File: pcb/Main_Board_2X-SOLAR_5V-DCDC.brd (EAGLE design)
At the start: 82.6 x 29.8 mm, 32 parts, among them T2 MMUN2133LT1G, U1 LTC4015EUHFPBFQFN-38_UHF-M, U3 TPS61090RSAR, X1 6V_PV, X2 5V output

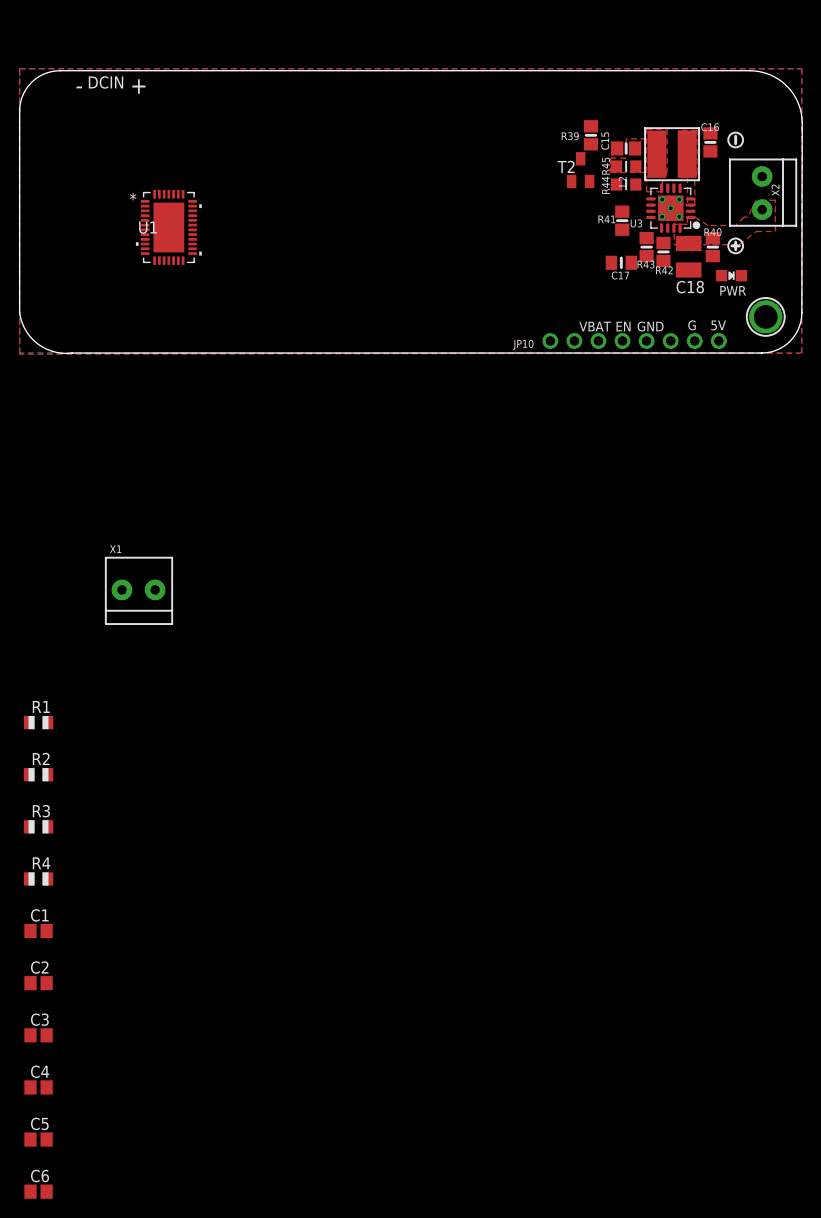
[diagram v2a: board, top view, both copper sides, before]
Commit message: Updated BOM and layout for LTC4015
Schematic pinout redone for LTC4015 part to match design application guide and make schematic easier to follow. Schematic and board routing started. BOM updated and consolidated for last revision of board (non-LTC)
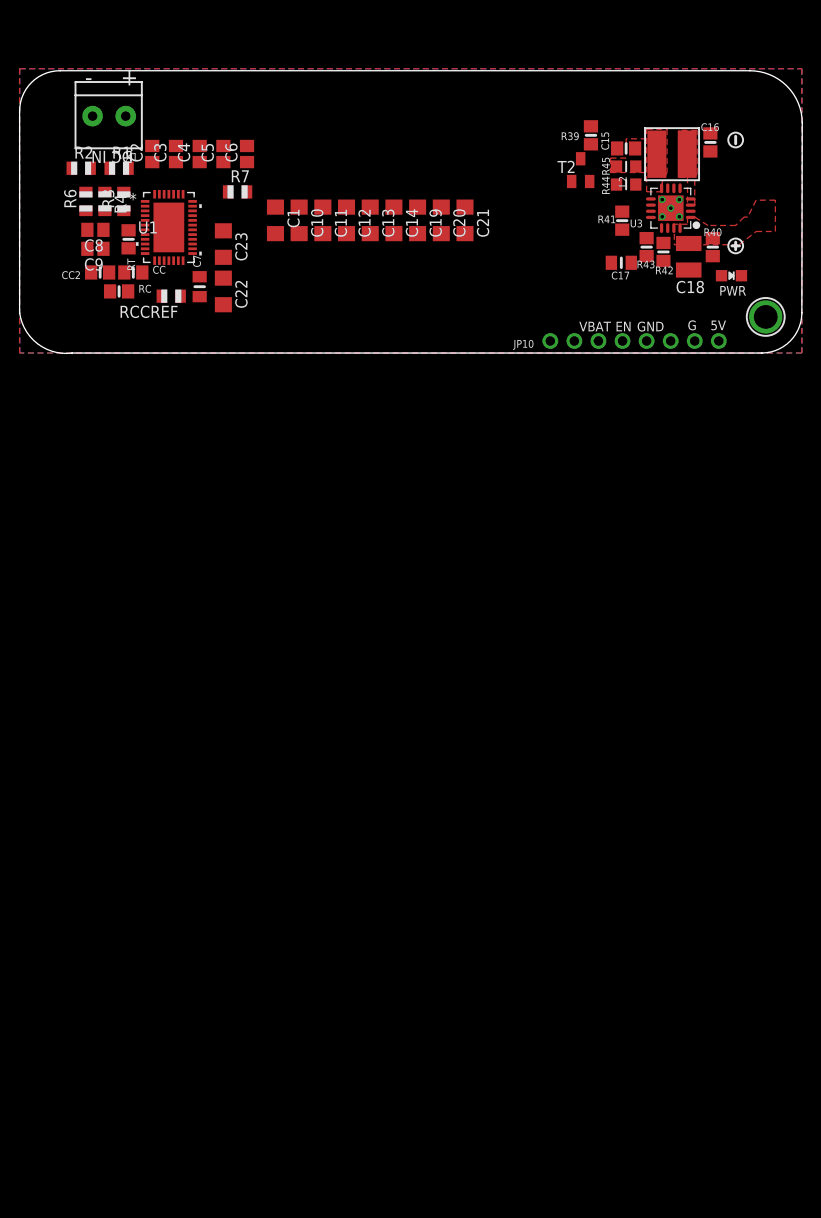
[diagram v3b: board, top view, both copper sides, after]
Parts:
- removed X2: 5V output, microbuilder:TERMBLOCK_1X2-3.5MM
- added C10, C11, C12, C13, C14, C19, C20, C22: 10 uF, resistor:C1206
- added C21, C23: 0.1 uF, resistor:C1206
- added C7: 0.1uF, microbuilder:0805_10MGAP
- added C8: 0.1 uF, adafruit:C0805
- added C9: 10 uF, adafruit:C0805
- added CC: 0.22 uF, microbuilder:0805-NO
- added CC2: 0.01 uF, microbuilder:0805-NO
- added R6, R7: 10k, adafruit:R0805
- added RC: 200, microbuilder:0805-NO
- added RCCREF: 301k, adafruit:R0805
- added RT: 95.3k, microbuilder:0805-NO
- C1: value (none) -> 10 uF; device adafruit:C0805 -> resistor:C1206
- C2, C3, C4, C5: value (none) -> 10 uF
- C6: value (none) -> 100 pF
- R1: value (none) -> 47k
- R2: value (none) -> 10k
- R3: value (none) -> 226k
- R4: value (none) -> 64.9k
- moved C6 111.7 mm to (24.0, 21.0), turned to 90 degrees
- moved C5 105.8 mm to (21.5, 21.0), turned to 90 degrees
- moved C4 100.0 mm to (19.0, 21.0), turned to 90 degrees
- moved C3 94.1 mm to (16.5, 21.0), turned to 90 degrees
- moved C2 88.3 mm to (14.0, 21.0), turned to 90 degrees
- moved C1 79.1 mm to (27.0, 14.0), turned to 270 degrees
- moved R4 71.8 mm to (9.00, 16.0), turned to 270 degrees
- moved R3 66.6 mm to (11.0, 16.0), turned to 90 degrees
- moved R2 64.2 mm to (6.50, 19.5)
- moved R1 59.1 mm to (10.5, 19.5)
- moved X1 50.1 mm to (9.50, 25.0), turned to 180 degrees
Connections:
- net N$42 renamed FB
- net N$44 renamed LED+
- removed net GND_2: U1.14
- removed net SGND: U1.7
- new net INTVCC: C8.1, C9.1, U1.27, U1.28, U1.36, U1.38
- new net N$1: C6.1, R7.2, U1.8
- new net N$11: CC.2, RC.2
- new net N$12: C23.1, U1.25
- new net N$2: C2.1, C3.1, C4.1, C5.1, R1.2, R3.2, U1.35, X1.1
- new net N$3: R3.1, R4.2
- new net N$4: R4.1, R6.2, R7.1
- new net N$5: R1.1, R2.2
- new net N$6: C7.1, RCCREF.1, U1.17
- new net N$8: RT.2, U1.10
- new net N$9: CC.1, CC2.1, U1.9
- new net SCL: U1.4
- new net SDA: U1.5
- new net SMBALERT: U1.6
- new net SYS: C1.1, C10.1, C11.1, C12.1, C13.1, C14.1, C15.1, C17.1, C19.1, C20.1, C21.1, L2.P$1, R45.2, U1.31, U3.8
- net 5.0V: no longer X2.2
- net GND: now also C1.2, C10.2, C11.2, C12.2, C13.2, C14.2, C19.2, C2.2, C20.2, C21.2, C23.2, C3.2, C4.2, C5.2, C6.2, C7.2, C8.2, C9.2, CC2.2, R2.1, R6.1, RC.1, RCCREF.2, RT.1, U1.14, U1.23, U1.37, U1.7, X1.2; no longer X1.1, X2.1
- net VBAT: no longer C15.1, C17.1, L2.P$1, R45.2, U3.8
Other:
- board text added: "DC IN"
- board text removed: "DCIN"

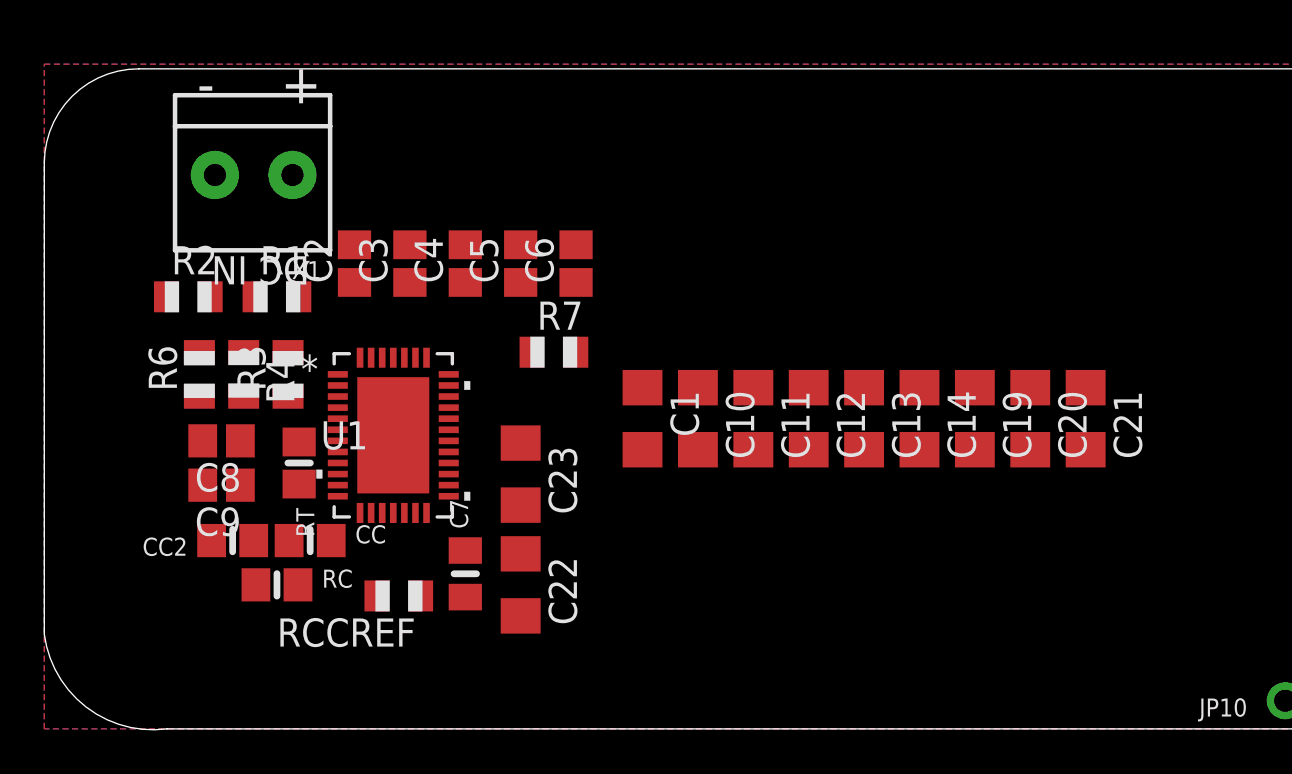
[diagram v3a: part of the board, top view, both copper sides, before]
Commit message: Updated library, schematic, and board layout
Added new components to library and continuing to update schematic and board
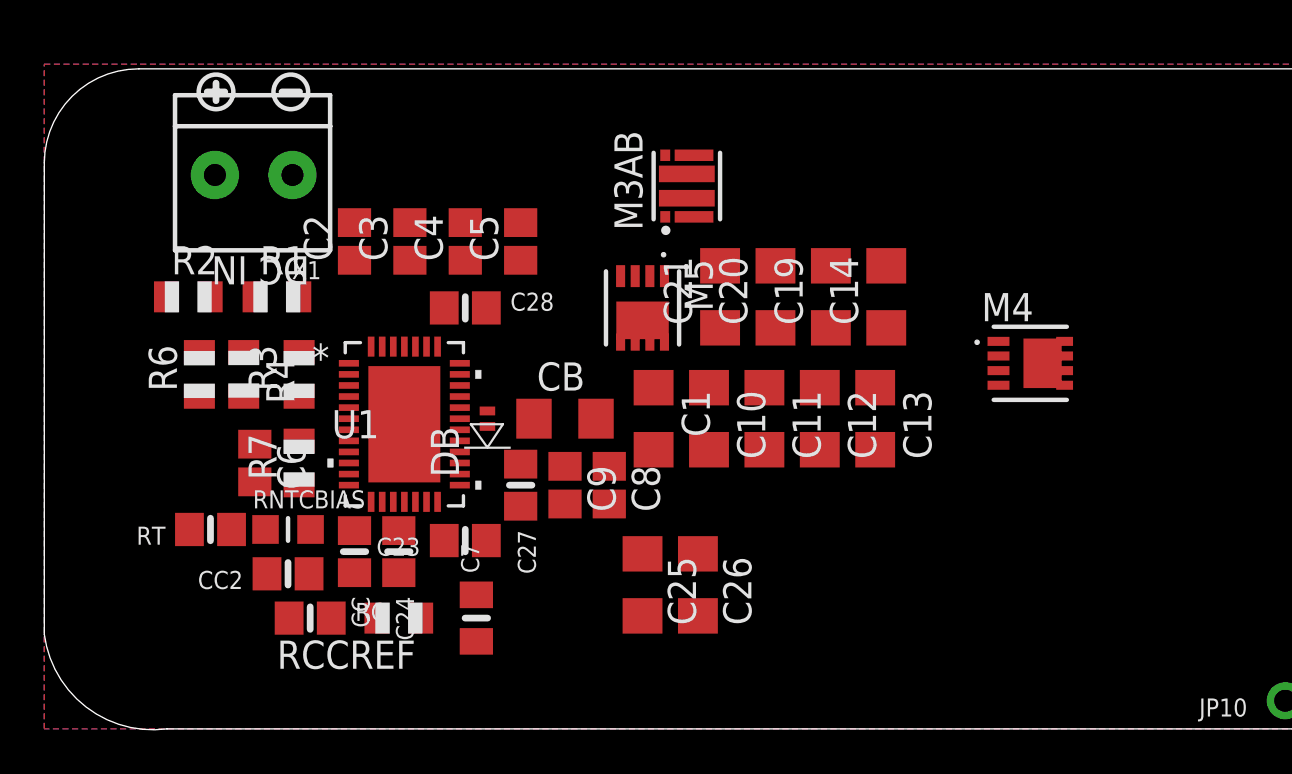
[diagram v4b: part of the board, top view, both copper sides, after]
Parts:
- removed C22: 10 uF, resistor:C1206
- added C24: 0.33 uF, microbuilder:0805-NO
- added C25, C26: 10 uF, adafruit:C1206
- added C27: 2.2 uF, microbuilder:0805-NO
- added C28: 1000 pF, microbuilder:0805-NO
- added CB: 0.47 uF, resistor:C1206
- added DB: 1N4448HLP, RCT:DO214AC
- added M3AB: FDMC8030, FDMC8030:TRANS_FDMC8030
- added M4: SI7611DN, Si7611DN:POWERPAK_1212_8
- added M5: FDMC8327L, RCT:8-POWER_W_DFN
- added RNTCBIAS: 10k, microbuilder:_0805MP
- added U$13: (no value), microbuilder:SYMBOL_MINUS
- added U$2: (no value), microbuilder:SYMBOL_PLUS
- C23: value 0.1 uF -> 1000 pF; device resistor:C1206 -> microbuilder:0805-NO
- moved C8 17.6 mm to (25.5, 11.0), turned to 270 degrees
- moved C21 17.4 mm to (30.5, 19.5), turned to 90 degrees
- moved C6 17.1 mm to (9.50, 12.0), turned to 270 degrees
- moved C9 15.5 mm to (23.5, 11.0), turned to 270 degrees
- moved C20 12.7 mm to (33.0, 19.5), turned to 90 degrees
- moved R7 12.5 mm to (11.5, 12.0), turned to 90 degrees
- moved C19 8.51 mm to (35.5, 19.5), turned to 90 degrees
- moved C14 5.70 mm to (38.0, 19.5), turned to 90 degrees
- moved RT 5.00 mm to (7.50, 9.00), turned to 180 degrees
- moved C23 3.91 mm to (19.0, 8.50), turned to 180 degrees
- moved CC2 2.92 mm to (11.0, 7.00)
- moved RC 2.12 mm to (12.0, 5.00)
- moved C7 2.06 mm to (19.5, 5.00)
- moved CC 2.06 mm to (14.0, 8.00), turned to 270 degrees
- moved C2 1.00 mm to (14.0, 22.0)
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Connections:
- net N$1 renamed UVCLFB
- new net BAT: C25.1, C26.1, U1.18
- new net BG: M3AB.8, U1.26
- new net CSN: C23.2, U1.19
- new net CSP: C23.1, C24.2, U1.20
- new net CSPM5: C24.1, U1.15
- new net INFET: M5.4, U1.34
- new net N$10: RNTCBIAS.2, U1.12
- new net N$13: CB.1, DB.C, U1.25
- new net N$14: C28.2, U1.32
- new net N$15: C28.1, U1.33
- new net N$7: C27.1, U1.22
- new net OUTFET: M4.4, U1.29
- new net SYSM5_DRAIN_2: M3AB.10, U1.30
- new net TG: M3AB.1, U1.24
- new net VIN: C2.1, C3.1, C4.1, C5.1, M5.1, M5.2, M5.3, R1.2, R3.2, U1.35, X1.1
- net GND: now also C25.2, C26.2, C27.2, M3AB.5, RNTCBIAS.1, U1.11; no longer C23.2, C7.2, RCCREF.2, U1.23
- net INTVCC: now also DB.A
- net N$12: now also CB.2, M3AB.4, M3AB.9, M4.1, M4.2, M4.3, U1.23; no longer C23.1, U1.25
- net N$2: now also C7.2, RCCREF.2, U1.16; no longer C2.1, C3.1, C4.1, C5.1, R1.2, R3.2, U1.35, X1.1
- net SYS: now also M4.5, M4.6, M4.7, M4.8, M5.10, M5.5, M5.6, M5.7, M5.8
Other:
- board text removed: "+"
- board text removed: "-"

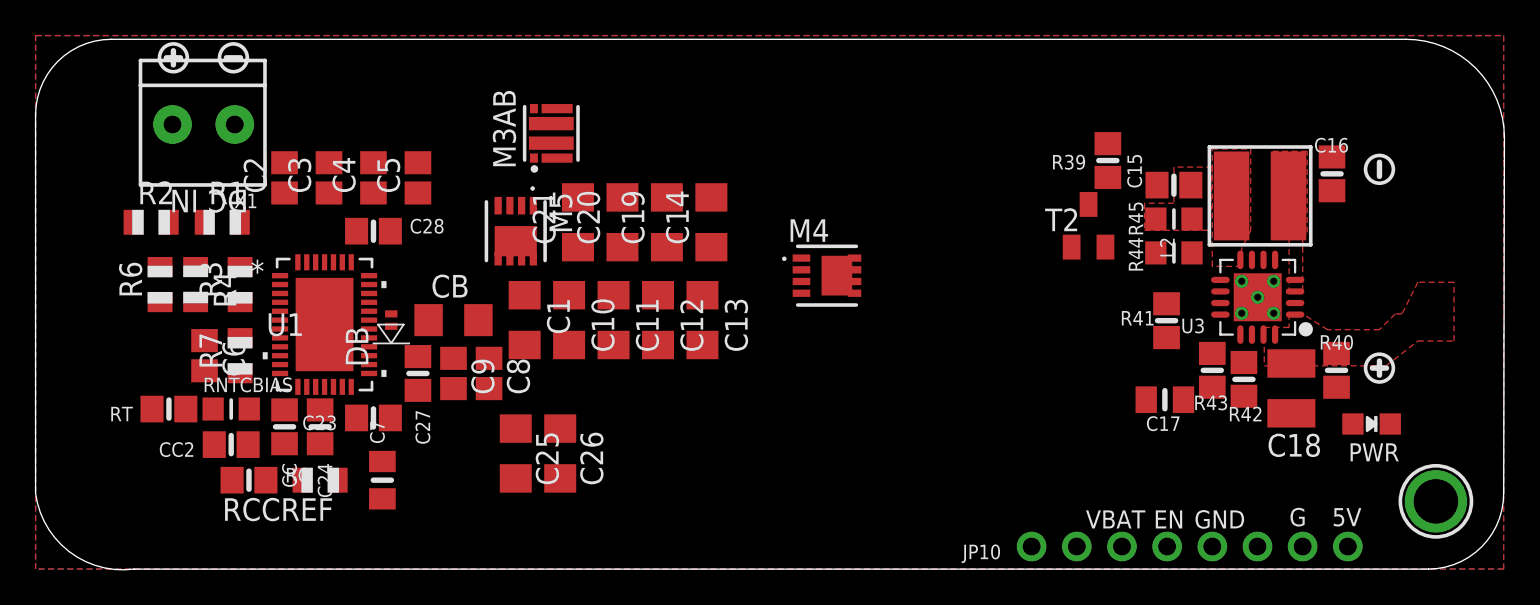
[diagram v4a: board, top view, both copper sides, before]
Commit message: New BOM for LiFePO4 board and updated sch/brd
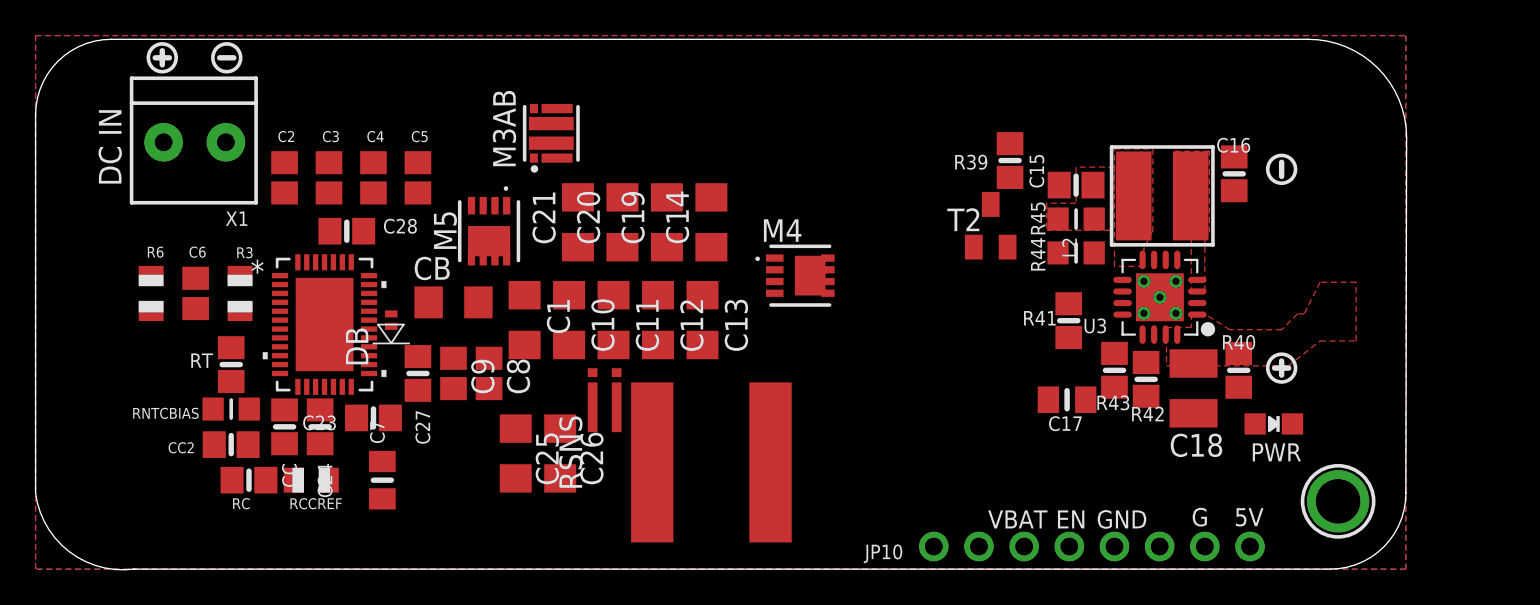
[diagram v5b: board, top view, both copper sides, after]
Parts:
- removed R1: 47k, adafruit:R0805
- removed R2, R7: 10k, adafruit:R0805
- removed R4: 64.9k, adafruit:R0805
- added FRAME1: FRAME-LEDGER, SparkFun-Aesthetics:CREATIVE_COMMONS
- added RSNS: KRL3216T4A-M-R004-F-T1, RCT:4-TERM-RESISTOR-SUMUSU
- added U$4: XAL1010-103ME-103ME, RCT:XAL1010
- R3: value 226k -> 200k
- R6: value 10k -> 50k
- moved JP10 5.50 mm to (59.4, 1.27)
- moved L2 5.50 mm to (63.4, 21.0)
- moved U3 5.50 mm to (63.2, 15.3)
- moved C16 5.50 mm to (67.4, 22.2)
- moved C17 5.50 mm to (58.0, 9.53)
- moved C18 5.50 mm to (65.1, 10.2)
- moved LED4 5.50 mm to (69.6, 8.16)
- moved R39 5.50 mm to (54.8, 23.0)
- moved R40 5.50 mm to (67.7, 11.2)
- moved R41 5.50 mm to (58.1, 14.0)
- moved R43 5.50 mm to (60.7, 11.2)
- moved T2 5.50 mm to (53.7, 19.3)
- moved U$12 5.50 mm to (73.2, 3.81)
- moved U$86 5.50 mm to (70.1, 11.3)
- moved U$87 5.50 mm to (70.1, 22.5)
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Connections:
- net N$7 renamed 2P5VCC
- removed net N$3: R3.1, R4.2
- removed net N$4: R4.1, R6.2, R7.1
- removed net N$5: R1.1, R2.2
- new net EQ: U1.13
- new net N$1: M4.1, M4.2, M4.3, U$4.P$2
- net GND: now also U1.21; no longer R2.1
- net N$12: now also U$4.P$1; no longer M4.1, M4.2, M4.3
- net UVCLFB: now also R3.1, R6.2; no longer R7.2
- net VIN: no longer R1.2
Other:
- board size 82.6 x 29.8 mm -> 77.1 x 29.8 mm
- board text added: "LiFePO4 Batteries Only! 3.2 V nom / 3.6 V max"
- board text removed: "LiFePO4 Batteries Only! 3.2 V / 3.6 V"

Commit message: added more components
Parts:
- added C22: 1 uF, microbuilder:0805-NO
- added RSNSI: KRL3216T4A-M-R004-F-T1, RCT:4-TERM-RESISTOR-SUMUSU
- moved U$4 15.0 mm to (23.0, 5.00)
- moved C7 4.03 mm to (15.5, 4.50)
- moved C24 3.64 mm to (12.5, 7.00)
- moved CC 3.64 mm to (10.5, 7.00)
- moved CC2 3.64 mm to (7.50, 6.00)
- moved RC 3.64 mm to (8.50, 4.00)
- moved RCCREF 3.64 mm to (12.0, 4.00)
- moved RNTCBIAS 3.64 mm to (7.50, 8.00)
- moved C26 3.61 mm to (32.5, 8.50)
- moved C23 3.54 mm to (15.5, 8.00)
- moved RSNS 3.54 mm to (35.5, 9.00)
- moved C25 3.20 mm to (29.5, 8.50)
- moved C27 3.16 mm to (18.5, 12.0)
- moved T2 3.04 mm to (50.7, 18.8)
- moved C14 3.00 mm to (35.0, 19.5)
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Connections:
- net N$10 renamed NTCBIAS
- net N$12 renamed SW_LTC
- net N$2 renamed CCREFM
- net N$6 renamed CCREFP
- net N$8 renamed RT
- net N$9 renamed VC
- removed net N$14: C28.2, U1.32
- removed net N$15: C28.1, U1.33
- new net CLN: C22.1, C28.2, U1.32
- new net CLP: C28.1, RSNSI.P$3, U1.33
- new net N$3: M5.10, M5.5, M5.6, M5.7, M5.8, RSNSI.P$1
- net BAT: now also RSNS.P$2
- net CSN: now also RSNS.P$4
- net CSP: now also RSNS.P$3
- net N$1: now also RSNS.P$1
- net SYS: now also C22.2, RSNSI.P$2; no longer M5.10, M5.5, M5.6, M5.7, M5.8
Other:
- board size 77.1 x 29.8 mm -> 74.1 x 29.8 mm

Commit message: Sch/Brd update, added image for silkscreen
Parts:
- added C29: 120 uF, microbuilder:0805-NO
- added C30: 0.33 uF, microbuilder:0805-NO
- added CN5: USBA_FEMALE, microbuilder:USB_HOST-PTH
- added R35: 43K, microbuilder:0805-NO
- added R36: 49.9K, microbuilder:0805-NO
- added R37: 75K 1%, microbuilder:0805-NO
- added R38: 49.9K 1%, microbuilder:0805-NO
- moved FRAME1 28.0 mm to (0.00, 0.00)
- moved M3AB 12.8 mm to (19.5, 13.5), turned to 180 degrees
- moved RC 9.01 mm to (3.50, 11.5), turned to 90 degrees
- moved C25 7.16 mm to (36.0, 5.50)
- moved CC 6.80 mm to (6.50, 12.5), turned to 180 degrees
- moved C26 6.71 mm to (38.5, 5.50)
- moved RSNSI 6.58 mm to (26.5, 19.0)
- moved DB 6.52 mm to (22.5, 17.5)
- moved CB 5.94 mm to (24.4, 10.5), turned to 180 degrees
- moved RCCREF 4.74 mm to (13.5, 8.50)
- moved CC2 4.61 mm to (6.50, 10.5)
- moved M4 4.00 mm to (40.0, 12.5), turned to 90 degrees
- moved RSNS 3.16 mm to (32.5, 8.00), turned to 90 degrees
- moved RNTCBIAS 3.00 mm to (10.5, 8.00), turned to 90 degrees
- moved U$4 3.00 mm to (26.0, 5.00)
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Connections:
- removed net SYSM5_DRAIN_2: M3AB.10, U1.30
- new net D+1: CN5.D+, R37.1, R38.1
- new net D-1: CN5.D-, R35.1, R36.1
- new net N$2: C30.2, U1.30
- new net N$4: C30.1, M3AB.10
- net 5.0V: now also CN5.VBUS, R35.2, R37.2
- net CLN: now also RSNSI.P$4
- net GND: now also C29.1, CN5.GND, R36.2, R38.2
- net SYS: now also C29.2
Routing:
- net SW_LTC: track 0.00 -> 16.0 mm
- net UVCLFB: track 0.00 -> 8.32 mm
- net TG: track 0.00 -> 6.47 mm
- net VC: track 0.00 -> 5.30 mm
- net EQ: track 0.00 -> 5.06 mm
- net CSP: track 0.00 -> 4.25 mm
- net VIN: track 0.00 -> 4.00 mm
- net CLN: track 0.00 -> 3.85 mm
- net 2P5VCC: track 0.00 -> 3.60 mm
- net BG: track 0.00 -> 3.15 mm
- net NTCBIAS: track 0.00 -> 2.94 mm
- net CSN: track 0.00 -> 2.08 mm
- net CLP: track 0.00 -> 2.08 mm
- net N$11: track 0.00 -> 2.07 mm
- added copper zone on layer 1, net CLN
- added copper zone on layer 1, net SW_LTC
- added copper zone on layer 1, net SYS
- added copper zone on layer 1, net VIN
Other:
- board size 74.1 x 29.8 mm -> 75.6 x 29.8 mm
- board text added: "VBUS"
- board text removed: "G"
